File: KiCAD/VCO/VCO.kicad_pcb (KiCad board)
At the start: 2 copper layers, 50 x 100 mm, 41 parts, among them J1 CV IN 1, J2 CV IN 2, J3 PWM, J4 SAW OUT, J5 PULSE OUT, J6 Conn_01x03_Pin, J7 Conn_01x03_Pin, Q1 NPN, T1 PNP, T2 NPN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

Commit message: Add a cap to pin 13
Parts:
- added C4: 220nF, Capacitor_THT:C_Disc_D5.0mm_W2.5mm_P2.50mm, F.Cu at (82.8, 120.0)
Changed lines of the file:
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@@
 	(net 31 "Net-(R18-Pad2)")
 	(net 32 "Net-(U1-Pad4)")
-	(net 33 "Net-(U1-Pad10)")
+	(net 33 "Net-(C4-Pad2)")
 	(footprint "HackSynth:Potentiometer_Alps_RK09K_Horizontal"
 		(layer "F.Cu")
@@
 			(layers "*.Cu" "*.Mask")
 			(remove_unused_layers no)
-			(net 33 "Net-(U1-Pad10)")
+			(net 33 "Net-(C4-Pad2)")
 			(pintype "output")
 		)
@@
 			(layers "*.Cu" "*.Mask")
 			(remove_unused_layers no)
-			(net 33 "Net-(U1-Pad10)")
+			(net 33 "Net-(C4-Pad2)")
 			(pintype "input")
 		)
@@
 			(offset
 				(xyz 0 0 0)
+			)
+			(scale
+				(xyz 1 1 1)
+			)
+			(rotate
+				(xyz 0 0 0)
+			)
+		)
+	)
+	(footprint "Capacitor_THT:C_Disc_D5.0mm_W2.5mm_P2.50mm"
+		(layer "F.Cu")
+		(at 82.75 120 90)
+		(descr "C, Disc series, Radial, pin pitch=2.50mm, , diameter*width=5*2.5mm^2, Capacitor, http://cdn-reichelt.de/documents/datenblatt/B300/DS_KERKO_TC.pdf")
+		(tags "C Disc series Radial pin pitch 2.50mm  diameter 5mm width 2.5mm Capacitor")
+		(property "Reference" "C4"
+			(at 1.25 -2.500001 90)
+			(layer "F.SilkS")
+			(effects
+				(font
+					(size 1 1)
+					(thickness 0.15)
+				)
+			)
+		)
+		(property "Value" "220nF"
+			(at 1.25 2.500001 90)
+			(layer "F.Fab")
+			(effects
+				(font
+					(size 1 1)
+					(thickness 0.15)
+				)
+			)
+		)
+		(property "Datasheet" ""
+			(at 0 0 90)
+			(unlocked yes)
+			(layer "F.Fab")
+			(hide yes)
+			(effects
+				(font
+					(size 1.27 1.27)
+					(thickness 0.15)
+				)
+			)
+		)
+		(property "Description" "Unpolarized capacitor"
+			(at 0 0 90)
+			(unlocked yes)
+			(layer "F.Fab")
+			(hide yes)
+			(effects
+				(font
+					(size 1.27 1.27)
+					(thickness 0.15)
+				)
+			)
+		)
+		(property ki_fp_filters "C_*")
+		(sheetname "/")
+		(sheetfile "VCO.kicad_sch")
+		(attr through_hole)
+		(fp_line
+			(start 3.87 -1.37)
+			(end 3.87 1.37)
+			(stroke
+				(width 0.12)
+				(type solid)
+			)
+			(layer "F.SilkS")
+		)
+		(fp_line
+			(start -1.37 -1.37)
+			(end 3.87 -1.37)
+			(stroke
+				(width 0.12)
+				(type solid)
+			)
+			(layer "F.SilkS")
+		)
+		(fp_line
+			(start -1.37 -1.37)
+			(end -1.37 1.37)
+			(stroke
+				(width 0.12)
+				(type solid)
+			)
+			(layer "F.SilkS")
+		)
+		(fp_line
+			(start -1.37 1.37)
+			(end 3.87 1.37)
+			(stroke
+				(width 0.12)
+				(type solid)
+			)
+			(layer "F.SilkS")
+		)
+		(fp_line
+			(start 4 -1.5)
+			(end -1.5 -1.5)
+			(stroke
+				(width 0.05)
+				(type solid)
+			)
+			(layer "F.CrtYd")
+		)
+		(fp_line
+			(start -1.5 -1.5)
+			(end -1.5 1.5)
+			(stroke
+				(width 0.05)
+				(type solid)
+			)
+			(layer "F.CrtYd")
+		)
+		(fp_line
+			(start 4 1.5)
+			(end 4 -1.5)
+			(stroke
+				(width 0.05)
+				(type solid)
+			)
+			(layer "F.CrtYd")
+		)
+		(fp_line
+			(start -1.5 1.5)
+			(end 4 1.5)
+			(stroke
+				(width 0.05)
+				(type solid)
+			)
+			(layer "F.CrtYd")
+		)
+		(fp_line
+			(start 3.75 -1.25)
+			(end -1.25 -1.25)
+			(stroke
+				(width 0.1)
+				(type solid)
+			)
+			(layer "F.Fab")
+		)
+		(fp_line
+			(start -1.25 -1.25)
+			(end -1.25 1.25)
+			(stroke
+				(width 0.1)
+				(type solid)
+			)
+			(layer "F.Fab")
+		)
+		(fp_line
+			(start 3.75 1.25)
+			(end 3.75 -1.25)
+			(stroke
+				(width 0.1)
+				(type solid)
+			)
+			(layer "F.Fab")
+		)
+		(fp_line
+			(start -1.25 1.25)
+			(end 3.75 1.25)
+			(stroke
+				(width 0.1)
+				(type solid)
+			)
+			(layer "F.Fab")
+		)
+		(fp_text user "${REFERENCE}"
+			(at 1.25 0 90)
+			(layer "F.Fab")
+			(effects
+				(font
+					(size 1 1)
+					(thickness 0.15)
+				)
+			)
+		)
+		(pad "1" thru_hole circle
+			(at 0 0 90)
+			(size 1.6 1.6)
+			(drill 0.8)
+			(layers "*.Cu" "*.Mask")
+			(remove_unused_layers no)
+			(net 9 "GND")
+			(pintype "passive")
+		)
+		(pad "2" thru_hole circle
+			(at 2.5 0 90)
+			(size 1.6 1.6)
+			(drill 0.8)
+			(layers "*.Cu" "*.Mask")
+			(remove_unused_layers no)
+			(net 33 "Net-(C4-Pad2)")
+			(pintype "passive")
+		)
+		(embedded_fonts no)
+		(model "${KICAD9_3DMODEL_DIR}/Capacitor_THT.3dshapes/C_Disc_D5.0mm_W2.5mm_P2.50mm.wrl"
+			(offset
+				(xyz 0 0 0)

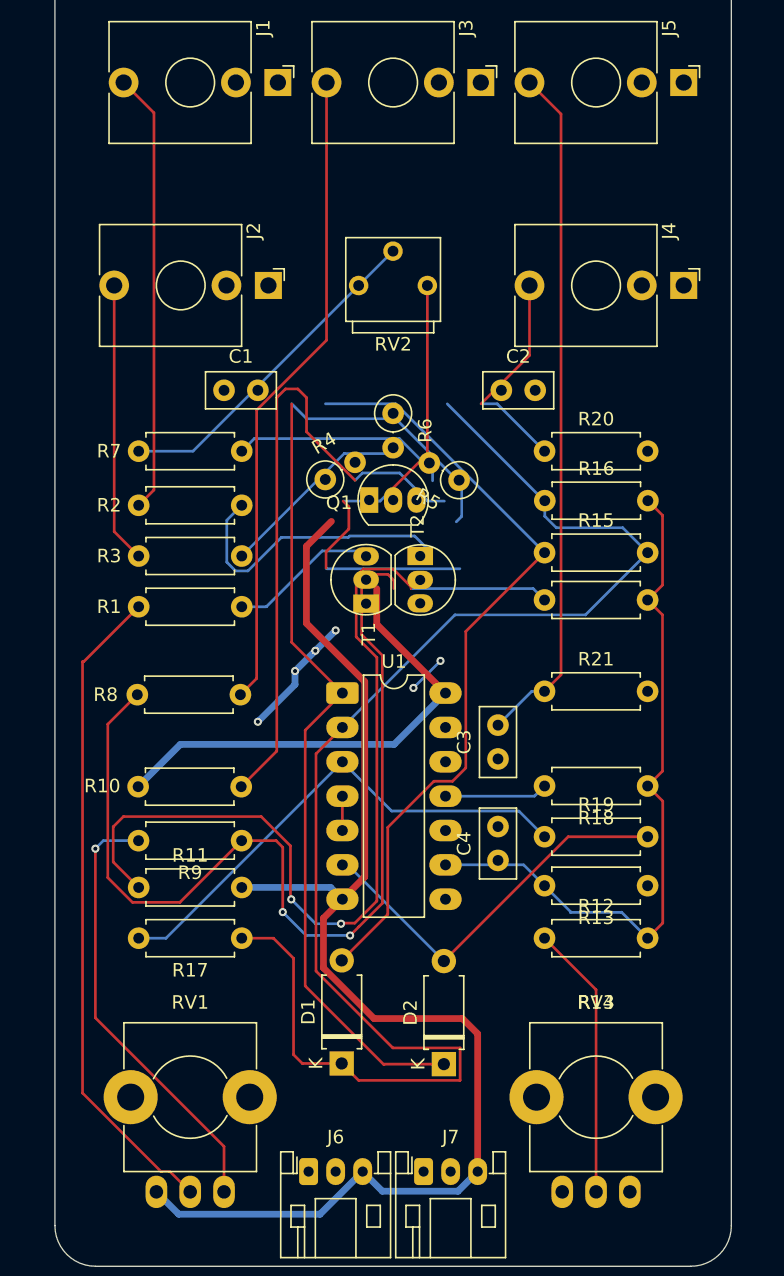
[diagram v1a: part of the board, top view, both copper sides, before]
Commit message: Rework VCO traces.
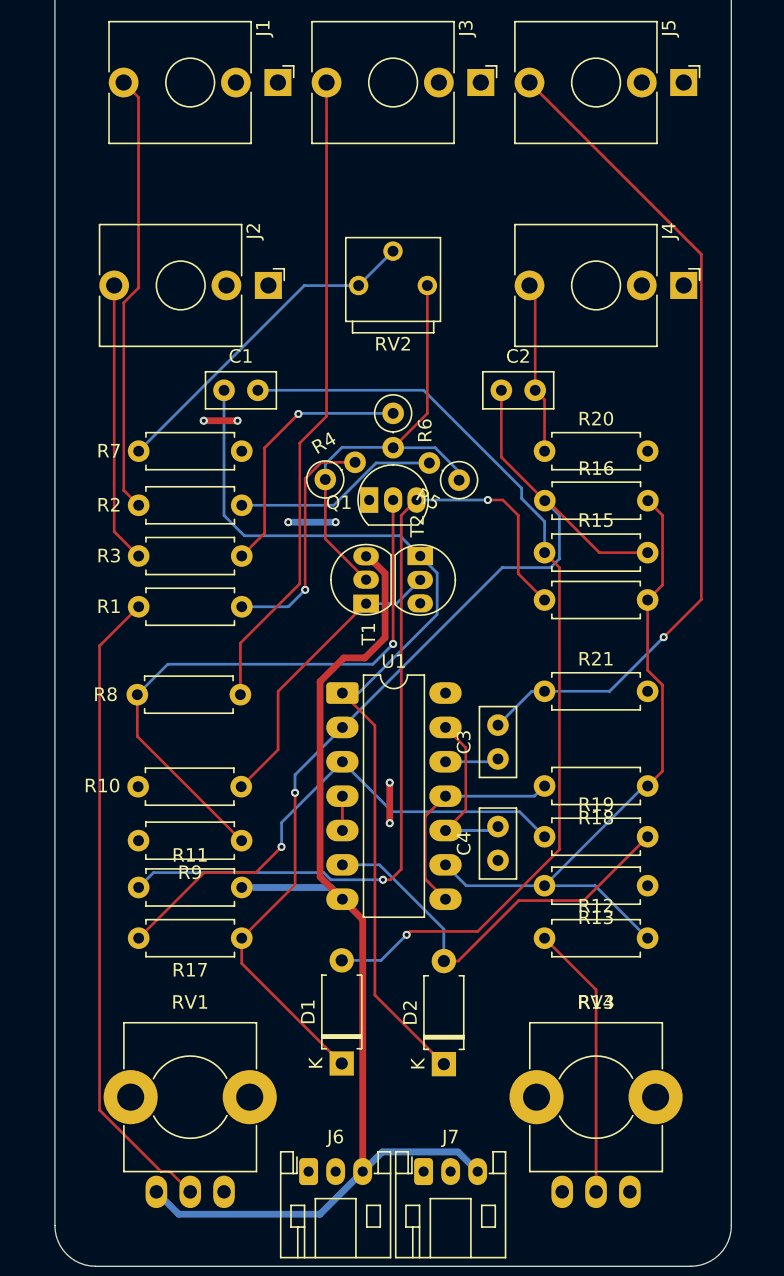
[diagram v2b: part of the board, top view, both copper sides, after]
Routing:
- net GND: track 58.0 -> 0.00 mm, vias 6 -> 0
- net Net-(D1-K): track 106.8 -> 75.6 mm, vias 0 -> 1
- net VDD: track 38.2 -> 9.00 mm, vias 1 -> 6
- net Net-(Q1-B): track 72.0 -> 45.1 mm, vias 2 -> 1
- net Net-(T1-C): track 40.2 -> 22.1 mm
- net Net-(Q1-E): track 78.9 -> 63.2 mm
- net Net-(C4-Pad2): track 0.00 -> 12.9 mm
- net Net-(D1-A): track 57.9 -> 69.9 mm, vias 0 -> 1
- net Net-(C3-Pad2): track 50.9 -> 62.4 mm, vias 0 -> 1
- net Net-(D2-K): track 58.4 -> 69.8 mm
- net VSS: track 95.2 -> 85.1 mm
- net Net-(T1-B): track 43.9 -> 34.6 mm
- net Net-(R18-Pad2): track 7.63 -> 16.5 mm
- net Net-(R2-Pad2): track 21.5 -> 15.2 mm
- net Net-(R3-Pad2): track 14.3 -> 19.3 mm, vias 0 -> 1
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
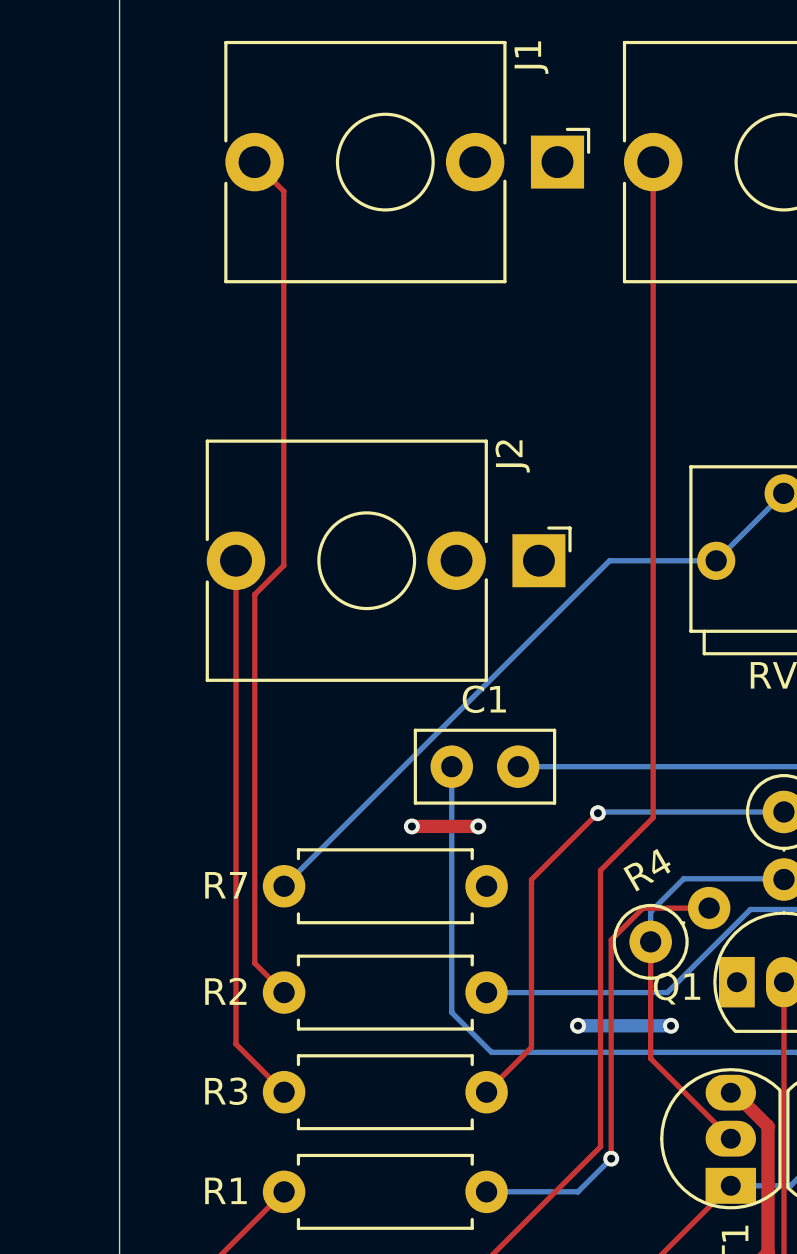
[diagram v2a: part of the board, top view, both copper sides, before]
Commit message: Bring jack back in line with grid
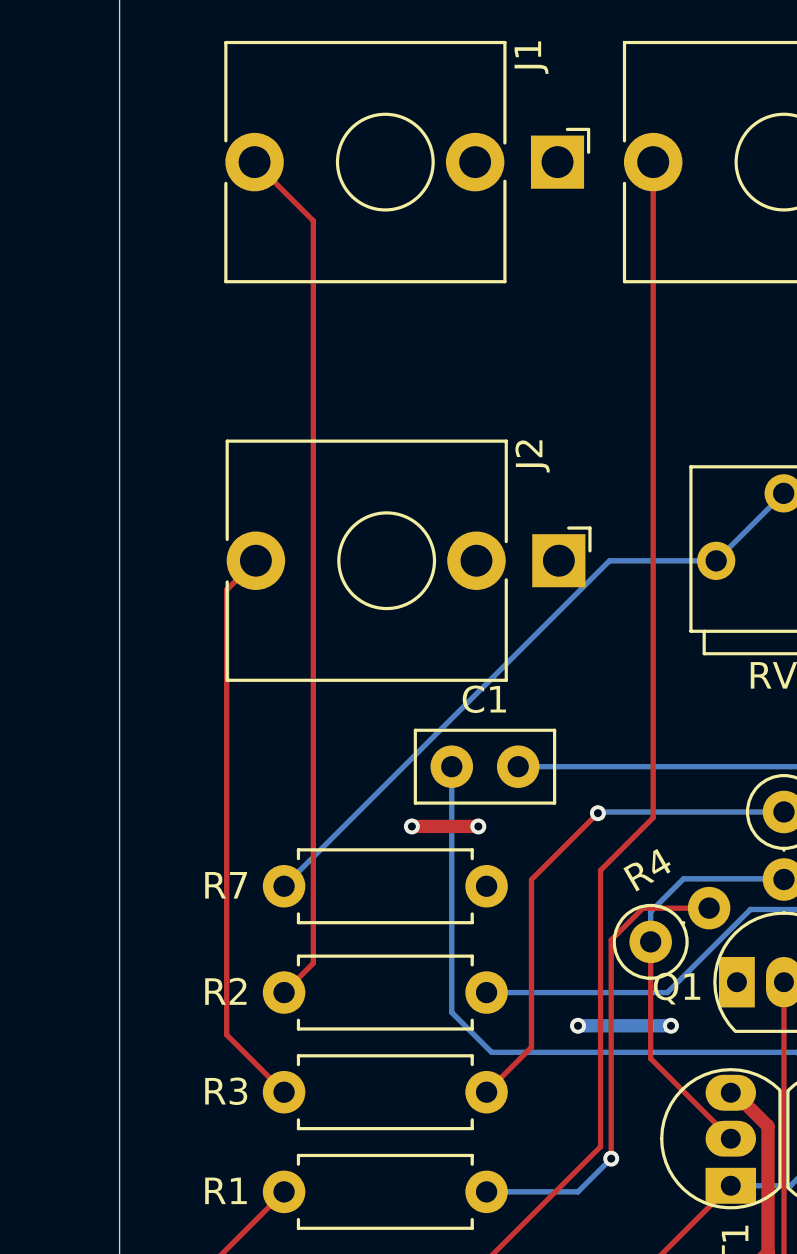
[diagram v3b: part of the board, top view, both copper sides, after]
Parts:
- moved J2 0.75 mm to (60.0, 77.5)
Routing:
- net Net-(J2-PadT): track 20.7 -> 21.4 mm
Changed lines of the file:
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@@
 	(footprint "HackSynth:Jack_3.5mm"
 		(layer "F.Cu")
-		(at 59.3 77.5 90)
+		(at 60.05 77.5 90)
 		(descr "TRS 3.5mm, vertical, Thonkiconn, PCB mount, (http://www.qingpu-electronics.com/en/products/WQP-PJ398SM-362.html)")
 		(tags "WQP-PJ398SM WQP-PJ301M-12 TRS 3.5mm mono vertical jack thonkiconn qingpu")
@@
 			(polygon
 				(pts
-					(xy 59.3 79.005141) (xy 59.545829 78.98493) (xy 59.785055 78.924841) (xy 60.011256 78.826486) (xy 60.218355 78.692508)
-					(xy 60.40079 78.526504) (xy 60.553664 78.332932) (xy 60.672869 78.116992) (xy 60.755206 77.884482)
-					(xy 60.798461 77.641646) (xy 60.801475 77.395007) (xy 60.764165 77.151187) (xy 60.687534 76.916734)
-					(xy 60.57364 76.697946) (xy 60.425542 76.500697) (xy 60.247216 76.330286) (xy 60.043452 76.191288)
-					(xy 59.819722 76.087436) (xy 59.582035 76.021519) (xy 59.336774 75.995308) (xy 59.090525 76.009507)
-					(xy 58.849901 76.063734) (xy 58.621366 76.156532) (xy 58.411055 76.285411) (xy 58.224618 76.446908)
-					(xy 58.067061 76.636687) (xy 57.942615 76.84965) (xy 57.854623 77.080079) (xy 57.805447 77.321785)
-					(xy 57.796408 77.568278) (xy 57.82775 77.812936) (xy 57.89863 78.049191) (xy 58.007144 78.270697)
-					(xy 58.150379 78.471505) (xy 58.324488 78.646223) (xy 58.524795 78.790158) (xy 58.745921 78.899445)
-					(xy 58.981926 78.971149) (xy 59.226474 79.003344)
+					(xy 60.05 79.005141) (xy 60.295829 78.98493) (xy 60.535055 78.924841) (xy 60.761256 78.826486)
+					(xy 60.968355 78.692508) (xy 61.15079 78.526504) (xy 61.303664 78.332932) (xy 61.422869 78.116992)
+					(xy 61.505206 77.884482) (xy 61.548461 77.641646) (xy 61.551475 77.395007) (xy 61.514165 77.151187)
+					(xy 61.437534 76.916734) (xy 61.32364 76.697946) (xy 61.175542 76.500697) (xy 60.997216 76.330286)
+					(xy 60.793452 76.191288) (xy 60.569722 76.087436) (xy 60.332035 76.021519) (xy 60.086774 75.995308)
+					(xy 59.840525 76.009507) (xy 59.599901 76.063734) (xy 59.371366 76.156532) (xy 59.161055 76.285411)
+					(xy 58.974618 76.446908) (xy 58.817061 76.636687) (xy 58.692615 76.84965) (xy 58.604623 77.080079)
+					(xy 58.555447 77.321785) (xy 58.546408 77.568278) (xy 58.57775 77.812936) (xy 58.64863 78.049191)
+					(xy 58.757144 78.270697) (xy 58.900379 78.471505) (xy 59.074488 78.646223) (xy 59.274795 78.790158)
+					(xy 59.495921 78.899445) (xy 59.731926 78.971149) (xy 59.976474 79.003344)
 				)
 			)
@@
 	)
 	(segment
-		(start 55.089 92.649)
-		(end 55.089 78.772314)
+		(start 57.291 64.711)
+		(end 55.08 62.5)
 		(width 0.2)
 		(layer "F.Cu")
@@
 	)
 	(segment
-		(start 56.179999 63.599999)
-		(end 55.08 62.5)
+		(start 56.19 93.75)
+		(end 57.291 92.649)
 		(width 0.2)
 		(layer "F.Cu")
@@
 	)
 	(segment
-		(start 55.089 78.772314)
-		(end 56.179999 77.681315)
+		(start 57.291 92.649)
+		(end 57.291 64.711)
 		(width 0.2)
 		(layer "F.Cu")
@@
 	)
 	(segment
-		(start 56.19 93.75)
-		(end 55.089 92.649)
-		(width 0.2)
-		(layer "F.Cu")
-		(net 10)
-	)
-	(segment
-		(start 56.179999 77.681315)
-		(end 56.179999 63.599999)
-		(width 0.2)
-		(layer "F.Cu")
-		(net 10)
-	)
-	(segment
-		(start 54.38 77.5)
-		(end 54.38 95.69)
+		(start 55.13 77.5)
+		(end 54.030001 78.599999)
 		(width 0.2)
 		(layer "F.Cu")
@@
 	)
 	(segment
-		(start 54.38 95.69)
+		(start 54.030001 95.340001)
 		(end 56.19 97.5)
 		(width 0.2)
 		(layer "F.Cu")
+		(net 11)
+	)
+	(segment
+		(start 54.030001 78.599999)
+		(end 54.030001 95.340001)
+		(width 0.2)
+		(layer "F.Cu")

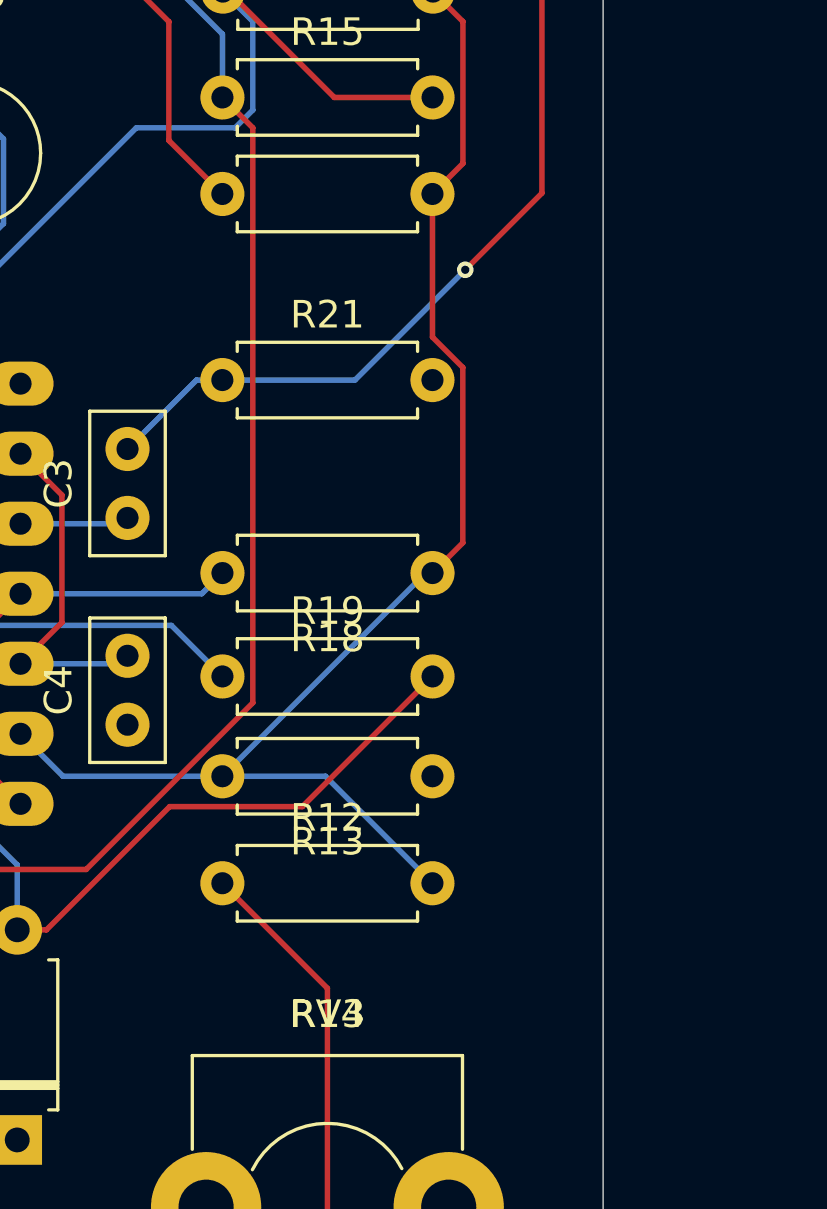
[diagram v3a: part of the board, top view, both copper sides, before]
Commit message: Chorus PCB Dread + Footprint Edit
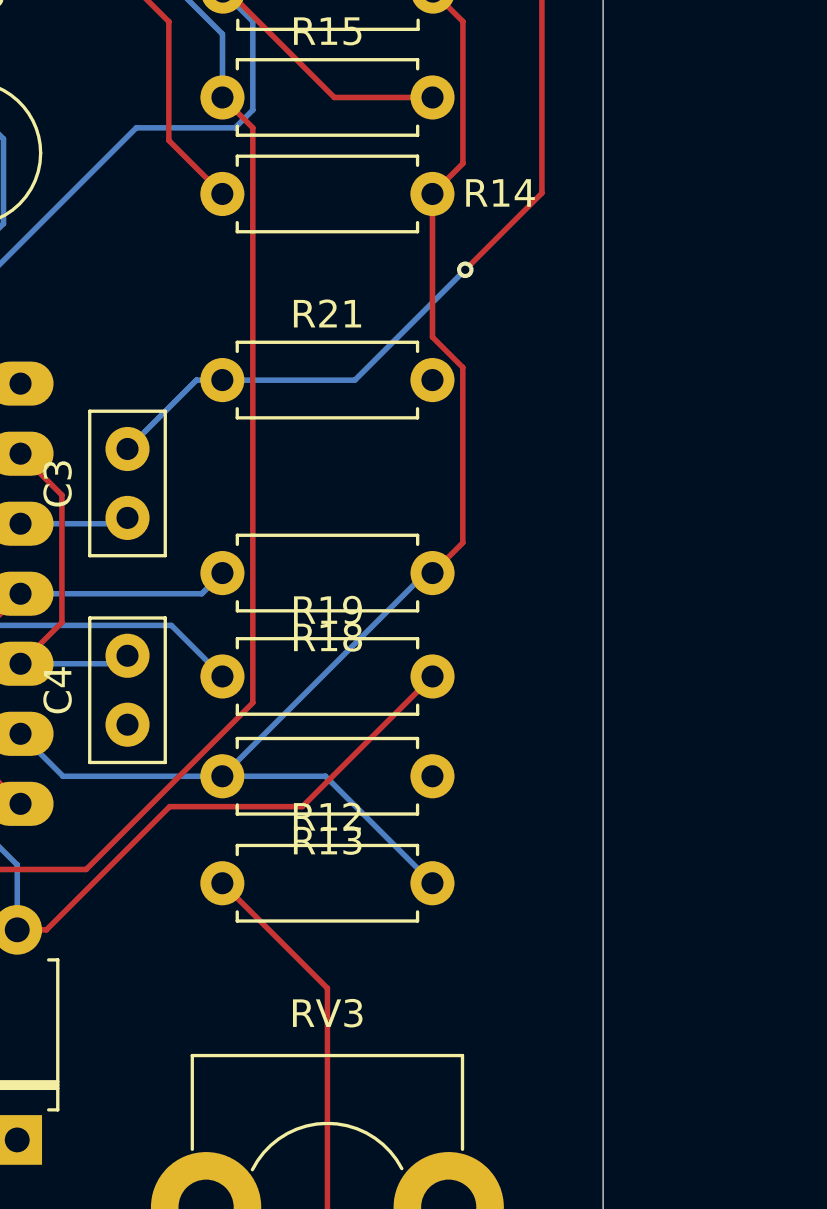
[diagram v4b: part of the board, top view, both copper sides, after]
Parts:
- U1: footprint Package_DIP:DIP-14_W7.62mm_LongPads -> HackSynth:DIP-14_W7.62mm_LongPads
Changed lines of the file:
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@@
 			(psa4output no)
 			(plot_black_and_white yes)
-			(plotinvisibletext no)
 			(sketchpadsonfab no)
 			(plotpadnumbers no)
@@
 		)
 	)
-	(footprint "Package_DIP:DIP-14_W7.62mm_LongPads"
+	(footprint "HackSynth:DIP-14_W7.62mm_LongPads"
 		(layer "F.Cu")
 		(at 71.25 107.63)
@@
 		)
 		(embedded_fonts no)
-		(model "${KICAD9_3DMODEL_DIR}/Package_DIP.3dshapes/DIP-14_W7.62mm_LongPads.wrl"
+		(model "C:/Users/ocd/OneDrive/Drafting/CCHS/HackSynth/KiCAD/HackSynth.pretty/DIP-14_W7.62mm.step"
 			(offset
 				(xyz 0 0 0)
@@
 		(tags "Resistor Axial_DIN0207 series Axial Horizontal pin pitch 7.62mm 0.25W = 1/4W length 6.3mm diameter 2.5mm")
 		(property "Reference" "R14"
-			(at 3.81 29.75 0)
+			(at 10.06 0 0)
 			(layer "F.SilkS")
 			(effects
